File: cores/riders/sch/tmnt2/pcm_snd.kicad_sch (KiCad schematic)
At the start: 42 parts, among them CN3 SOUND OUT, CN4 SOUND OUT, CN5 Conn_02x32_Row_Letter_First

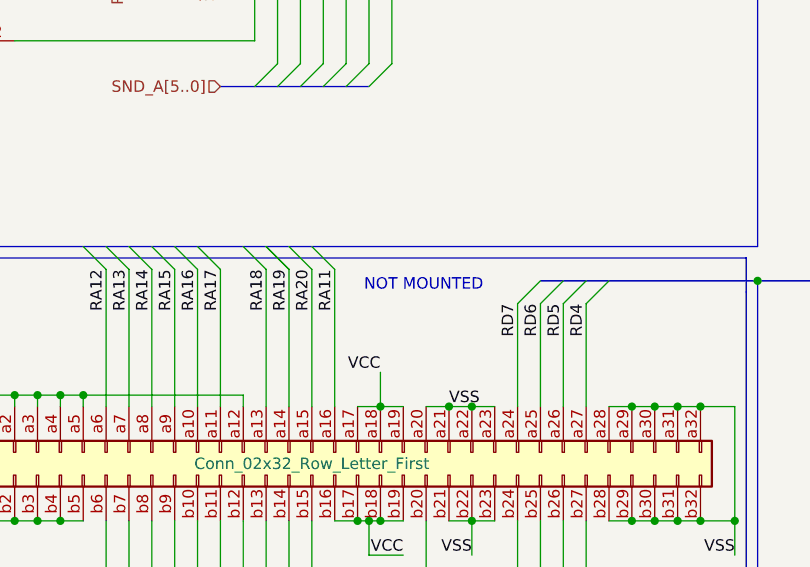
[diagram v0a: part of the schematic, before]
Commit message: sch: not mounted -> not populated
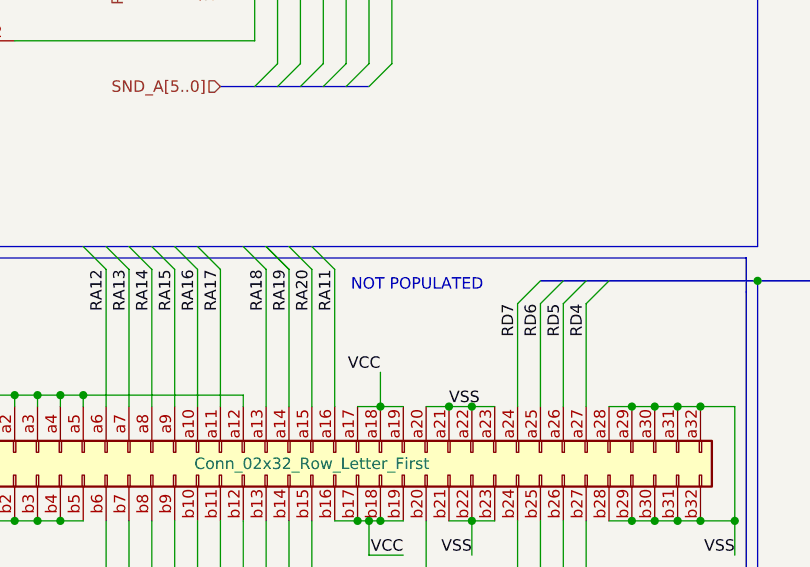
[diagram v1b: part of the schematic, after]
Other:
- note added: "NOT POPULATED"
- note removed: "NOT MOUNTED"
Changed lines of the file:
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@@
 		)
 	)
-	(text "NOT MOUNTED"
+	(text "NOT POPULATED"
 		(exclude_from_sim no)
 		(at 107.95 161.29 0)
